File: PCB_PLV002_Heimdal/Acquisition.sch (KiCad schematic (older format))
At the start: 6 parts, among them J2 ANALOG_IN_1, U8 LM2902

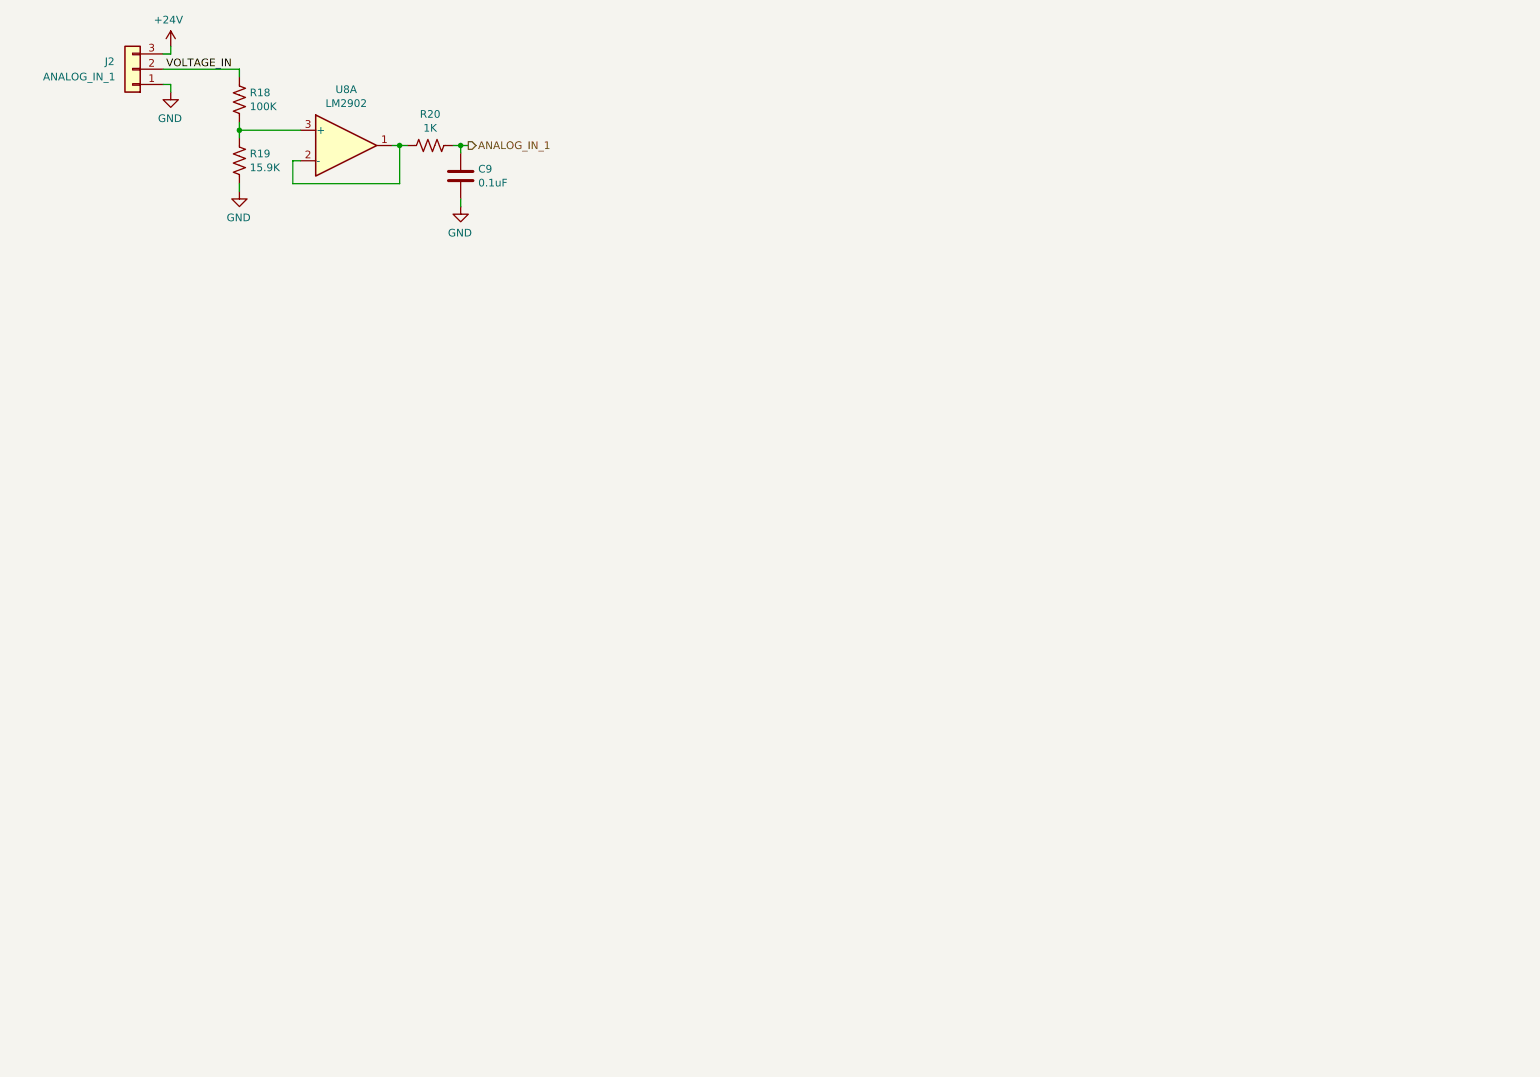
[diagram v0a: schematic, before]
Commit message: Most of sensors for heimdal complete, still need to sort out load cells, flammable gas
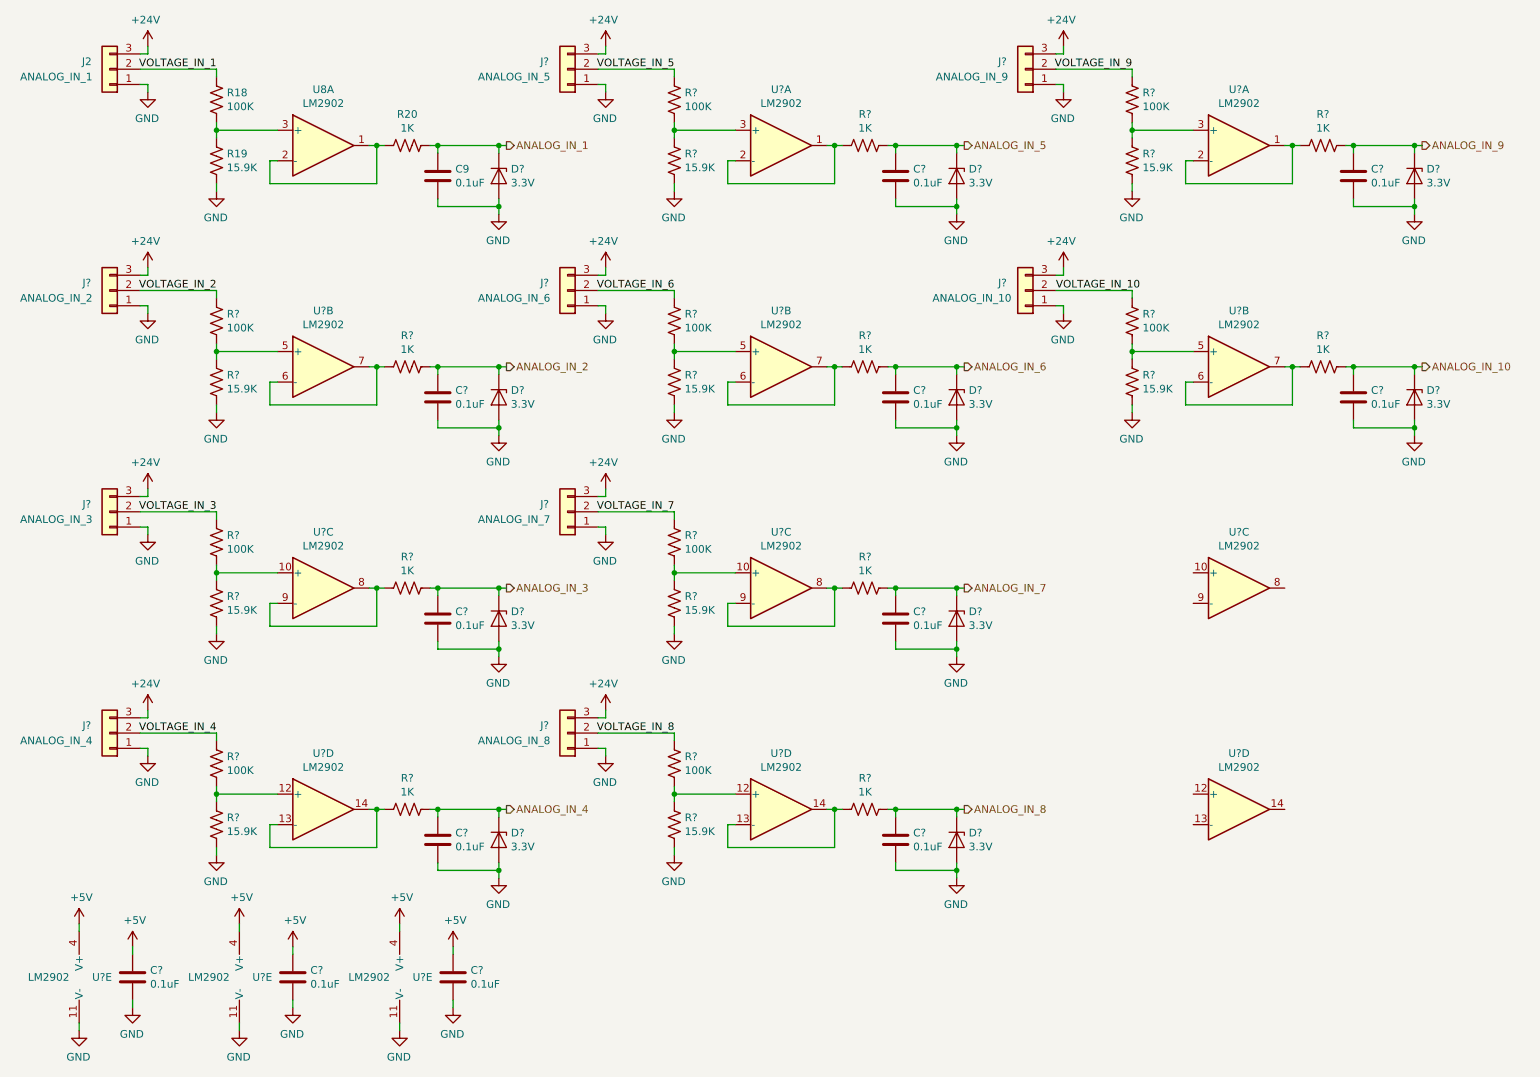
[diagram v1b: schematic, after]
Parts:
- added C? (x12): 0.1uF, Capacitor_SMD:C_0603_1608Metric_Pad1.05x0.95mm_HandSolder, symbol Device:C
- added D? (x10): 3.3V, symbol Device:D_Zener
- added J?: ANALOG_IN_2, symbol Connector_Generic:Conn_01x03
- added J?: ANALOG_IN_3, symbol Connector_Generic:Conn_01x03
- added J?: ANALOG_IN_4, symbol Connector_Generic:Conn_01x03
- added J?: ANALOG_IN_5, symbol Connector_Generic:Conn_01x03
- added J?: ANALOG_IN_6, symbol Connector_Generic:Conn_01x03
- added J?: ANALOG_IN_7, symbol Connector_Generic:Conn_01x03
- added J?: ANALOG_IN_8, symbol Connector_Generic:Conn_01x03
- added J?: ANALOG_IN_9, symbol Connector_Generic:Conn_01x03
- added J?: ANALOG_IN_10, symbol Connector_Generic:Conn_01x03
- added R? (x9): 100K, Resistor_SMD:R_0603_1608Metric_Pad1.05x0.95mm_HandSolder, symbol Device:R_US
- added R? (x9): 15.9K, Resistor_SMD:R_0603_1608Metric_Pad1.05x0.95mm_HandSolder, symbol Device:R_US
- added R? (x9): 1K, Resistor_SMD:R_0603_1608Metric_Pad1.05x0.95mm_HandSolder, symbol Device:R_US
- added U? (x14): LM2902, symbol Amplifier_Operational:LM2902
- R18, R19, R20: footprint (none) -> Resistor_SMD:R_0603_1608Metric_Pad1.05x0.95mm_HandSolder
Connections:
- net +24V: now also J?.3 (Pin_3), J?.3 (Pin_3), J?.3 (Pin_3), J?.3 (Pin_3), J?.3 (Pin_3), J?.3 (Pin_3), J?.3 (Pin_3), J?.3 (Pin_3), J?.3 (Pin_3)
- net ANALOG_IN_1: now also D?.1 (K)
- net GND: now also C?.2, C?.2, C?.2, C?.2, C?.2, C?.2, C?.2, C?.2, C?.2, C?.2, C?.2, C?.2, D?.2 (A), D?.2 (A), D?.2 (A), D?.2 (A), D?.2 (A), D?.2 (A), D?.2 (A), D?.2 (A), D?.2 (A), D?.2 (A), J?.1 (Pin_1), J?.1 (Pin_1), J?.1 (Pin_1), J?.1 (Pin_1), J?.1 (Pin_1), J?.1 (Pin_1), J?.1 (Pin_1), J?.1 (Pin_1), J?.1 (Pin_1), R?.2, R?.2, R?.2, R?.2, R?.2, R?.2, R?.2, R?.2, R?.2, U?.11 (V-), U?.11 (V-), U?.11 (V-)
- net VOLTAGE_IN renamed VOLTAGE_IN_1
- new net: R?.1, R?.2, U?.5 (+) (x3)
- new net: R?.2, U?.6 (-), U?.7 (x3)
- new net: R?.1, R?.2, U?.10 (+) (x2)
- new net: R?.2, U?.8, U?.9 (-) (x2)
- new net: R?.1, R?.2, U?.12 (+) (x2)
- new net: R?.2, U?.13 (-), U?.14 (x2)
- new net: R?.2, U?.1, U?.2 (-) (x2)
- new net: R?.1, R?.2, U?.3 (+) (x2)
- new net +5V: C?.1, C?.1, C?.1, U?.4 (V+), U?.4 (V+), U?.4 (V+)
- new net ANALOG_IN_10: C?.1, D?.1 (K), R?.1
- new net ANALOG_IN_2: C?.1, D?.1 (K), R?.1
- new net ANALOG_IN_3: C?.1, D?.1 (K), R?.1
- new net ANALOG_IN_4: C?.1, D?.1 (K), R?.1
- new net ANALOG_IN_5: C?.1, D?.1 (K), R?.1
- new net ANALOG_IN_6: C?.1, D?.1 (K), R?.1
- new net ANALOG_IN_7: C?.1, D?.1 (K), R?.1
- new net ANALOG_IN_8: C?.1, D?.1 (K), R?.1
- new net ANALOG_IN_9: C?.1, D?.1 (K), R?.1
- new net VOLTAGE_IN_10: J?.2 (Pin_2), R?.1
- new net VOLTAGE_IN_2: J?.2 (Pin_2), R?.1
- new net VOLTAGE_IN_3: J?.2 (Pin_2), R?.1
- new net VOLTAGE_IN_4: J?.2 (Pin_2), R?.1
- new net VOLTAGE_IN_5: J?.2 (Pin_2), R?.1
- new net VOLTAGE_IN_6: J?.2 (Pin_2), R?.1
- new net VOLTAGE_IN_7: J?.2 (Pin_2), R?.1
- new net VOLTAGE_IN_8: J?.2 (Pin_2), R?.1
- new net VOLTAGE_IN_9: J?.2 (Pin_2), R?.1
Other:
- moved on the sheet: C9, J2, R18, R19, R20, U8A
